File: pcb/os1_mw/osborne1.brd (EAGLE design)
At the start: 147 x 100 mm, 19 parts

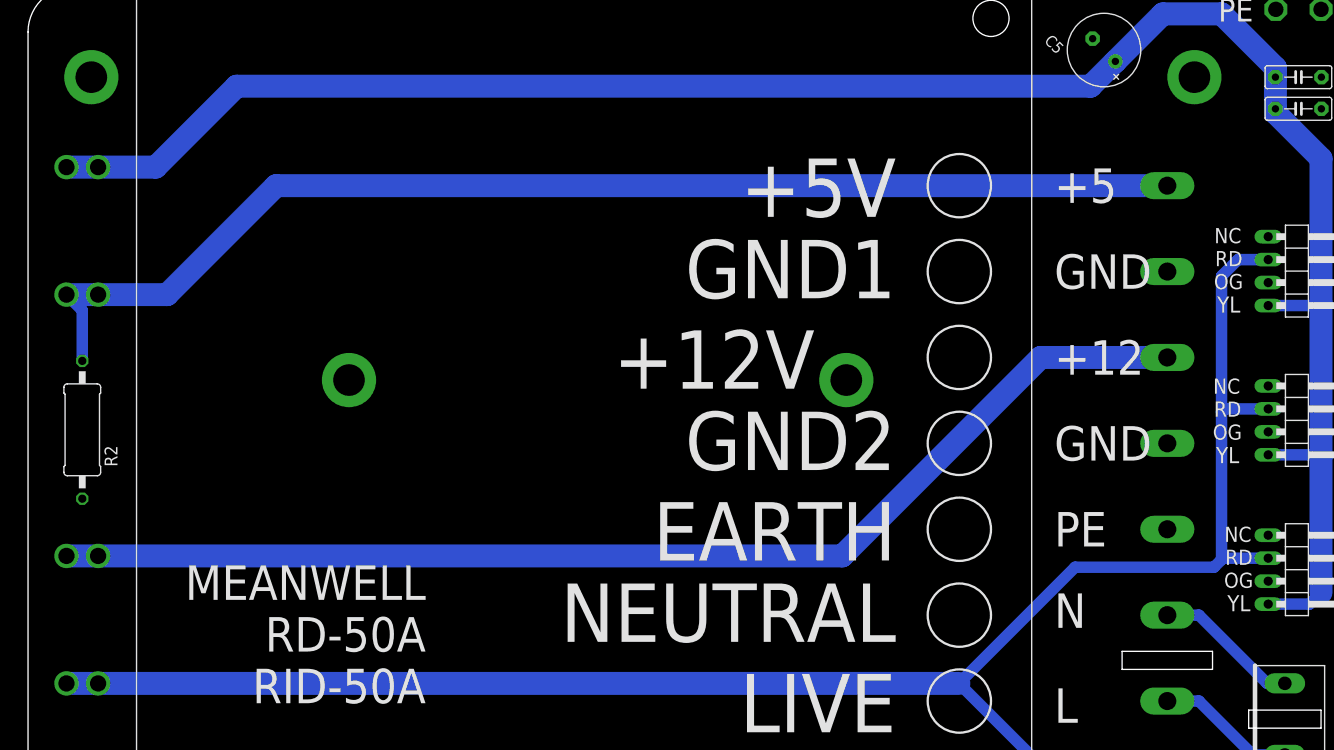
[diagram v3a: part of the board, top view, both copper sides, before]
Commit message: update os1 pcb
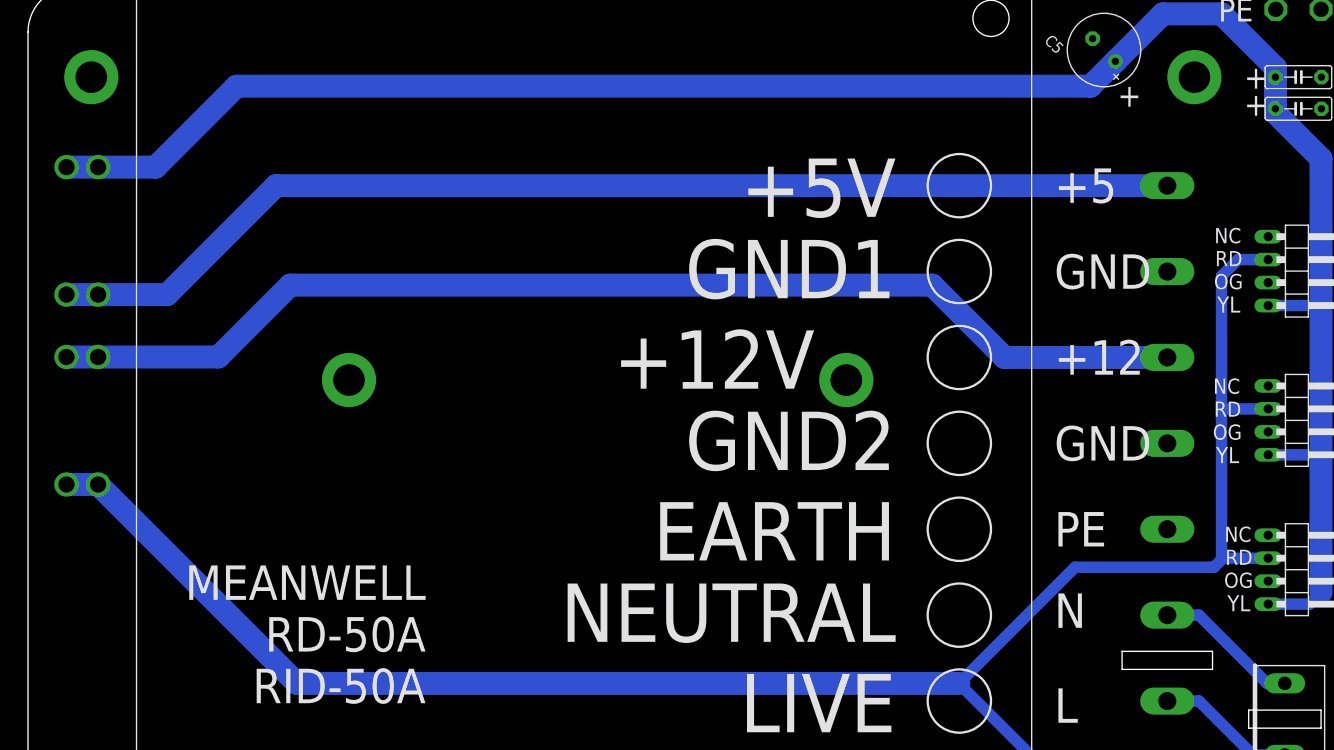
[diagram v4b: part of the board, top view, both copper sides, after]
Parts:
- removed R2: (no value), adafruit_changed:0411/15
- moved U$7 22.0 mm to (6.00, 52.0)
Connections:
- net GND: no longer R2.2
- net N$2: no longer R2.1
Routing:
- net +12V: track 207.7 -> 216.8 mm
- net N$2: track 134.8 -> 126.7 mm
- net N$1: track 130.8 -> 128.4 mm
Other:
- board text added: "+"
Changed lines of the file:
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@@
 <grid distance="1" unitdist="mm" unit="mm" style="lines" multiple="1" display="no" altdistance="1" altunitdist="mil" altunit="mil"/>
 <layers>
-<layer number="1" name="Top" color="4" fill="1" visible="no" active="yes"/>
+<layer number="1" name="Top" color="4" fill="1" visible="yes" active="yes"/>
 <layer number="2" name="Route2" color="16" fill="1" visible="no" active="no"/>
 <layer number="3" name="Route3" color="17" fill="1" visible="no" active="no"/>
@@
 <layer number="19" name="Unrouted" color="6" fill="1" visible="yes" active="yes"/>
 <layer number="20" name="Dimension" color="24" fill="1" visible="yes" active="yes"/>
-<layer number="21" name="tPlace" color="7" fill="1" visible="no" active="yes"/>
+<layer number="21" name="tPlace" color="7" fill="1" visible="yes" active="yes"/>
 <layer number="22" name="bPlace" color="7" fill="1" visible="yes" active="yes"/>
-<layer number="23" name="tOrigins" color="15" fill="1" visible="no" active="yes"/>
+<layer number="23" name="tOrigins" color="15" fill="1" visible="yes" active="yes"/>
 <layer number="24" name="bOrigins" color="15" fill="1" visible="yes" active="yes"/>
-<layer number="25" name="tNames" color="7" fill="1" visible="no" active="yes"/>
+<layer number="25" name="tNames" color="7" fill="1" visible="yes" active="yes"/>
 <layer number="26" name="bNames" color="7" fill="1" visible="yes" active="yes"/>
-<layer number="27" name="tValues" color="7" fill="1" visible="no" active="yes"/>
-<layer number="28" name="bValues" color="7" fill="1" visible="no" active="yes"/>
+<layer number="27" name="tValues" color="7" fill="1" visible="yes" active="yes"/>
+<layer number="28" name="bValues" color="7" fill="1" visible="yes" active="yes"/>
 <layer number="29" name="tStop" color="7" fill="3" visible="no" active="yes"/>
 <layer number="30" name="bStop" color="7" fill="6" visible="no" active="yes"/>
@@
 <layer number="37" name="tTest" color="7" fill="1" visible="no" active="yes"/>
 <layer number="38" name="bTest" color="7" fill="1" visible="no" active="yes"/>
-<layer number="39" name="tKeepout" color="4" fill="11" visible="no" active="yes"/>
+<layer number="39" name="tKeepout" color="4" fill="11" visible="yes" active="yes"/>
 <layer number="40" name="bKeepout" color="1" fill="11" visible="yes" active="yes"/>
-<layer number="41" name="tRestrict" color="4" fill="10" visible="no" active="yes"/>
+<layer number="41" name="tRestrict" color="4" fill="10" visible="yes" active="yes"/>
 <layer number="42" name="bRestrict" color="1" fill="10" visible="yes" active="yes"/>
 <layer number="43" name="vRestrict" color="2" fill="10" visible="no" active="yes"/>
@@
 <layer number="49" name="Reference" color="7" fill="1" visible="no" active="yes"/>
 <layer number="50" name="dxf" color="7" fill="1" visible="no" active="no"/>
-<layer number="51" name="tDocu" color="7" fill="1" visible="no" active="yes"/>
+<layer number="51" name="tDocu" color="7" fill="1" visible="yes" active="yes"/>
 <layer number="52" name="bDocu" color="7" fill="1" visible="yes" active="yes"/>
 <layer number="53" name="tGND_GNDA" color="7" fill="1" visible="no" active="no"/>
@@
 <text x="113.5" y="78" size="3.81" layer="25" align="center-left">+5</text>
 <polygon width="1.27" layer="41">
+<vertex x="1.75" y="61.5"/>
+<vertex x="10.25" y="61.5"/>
+<vertex x="10.25" y="40.5"/>
 <vertex x="1.75" y="40.5"/>
-<vertex x="10.25" y="40.5"/>
-<vertex x="10.25" y="19.5"/>
-<vertex x="1.75" y="19.5"/>
 </polygon>
 <polygon width="1.27" layer="41">
@@
 <rectangle x1="135" y1="18" x2="143" y2="20" layer="46"/>
 <rectangle x1="121" y1="24.5" x2="131" y2="26.5" layer="46"/>
-<text x="12.096" y="30.002" size="3.81" layer="26" rot="MR90" align="center">12V 3A</text>
+<text x="13.096" y="52.002" size="3.81" layer="26" rot="MR90" align="center">12V 3A</text>
 <text x="144.5" y="24" size="3.81" layer="25" align="center-left">N</text>
 <text x="144.5" y="14.5" size="3.81" layer="25" align="center-left">L</text>
@@
 <wire x1="141" y1="26" x2="139" y2="26" width="0.508" layer="22"/>
 <wire x1="139" y1="26" x2="132" y2="33" width="0.508" layer="22"/>
+<text x="120.5" y="88" size="2.54" layer="25" align="center-left">+</text>
+<text x="134.5" y="90" size="2.54" layer="25" align="center-left">+</text>
+<text x="134.5" y="87" size="2.54" layer="25" align="center-left">+</text>
 </plain>
 <attributes>
@@
 </element>
 <element name="JP4" library="appleii" package="1X04" value="" x="119.25" y="3.75" smashed="yes" rot="R180"/>
-<element name="R2" library="adafruit_changed" package="0411/15" value="" x="6" y="51" smashed="yes" rot="R270">
-<attribute name="NAME" x="9.889" y="46.92" size="1.4224" layer="25" ratio="10" rot="R90"/>
-<attribute name="VALUE" x="5.365" y="54.5814" size="1.27" layer="27" ratio="10" rot="R270"/>
-</element>
 <element name="U$3" library="os1" package="TERMINAL9500_MAINS" value="TERM_RD50_MAINS" x="126" y="78" smashed="yes" rot="R270"/>
 <element name="U$2" library="396_conn" package="396_2P_LIVE" value="396_2P_LIVE" x="139" y="19" smashed="yes" rot="R90"/>
-<element name="U$7" library="atx_power_control" package="FUSE_HOLDER_3IN1" value="CAR_FUSE_HOLDER3IN1" x="6" y="30" smashed="yes" rot="MR90"/>
+<element name="U$7" library="atx_power_control" package="FUSE_HOLDER_3IN1" value="CAR_FUSE_HOLDER3IN1" x="6" y="52" smashed="yes" rot="MR90"/>
 </elements>
 <signals>
@@
 <contactref element="U$4" pad="P$1"/>
 <contactref element="U$5" pad="P$1"/>
-<contactref element="R2" pad="2"/>
 <contactref element="U$1" pad="P$2"/>
 <contactref element="U$1" pad="P$1"/>
@@
 <contactref element="U$7" pad="A1"/>
 <contactref element="U$7" pad="A0"/>
-<wire x1="4.25" y1="22.95" x2="7.75" y2="22.95" width="2.54" layer="16"/>
-<wire x1="7.75" y1="22.95" x2="102.95" y2="22.95" width="2.54" layer="16"/>
+<wire x1="4.25" y1="44.95" x2="7.75" y2="44.95" width="2.54" layer="16"/>
 <wire x1="102.95" y1="22.95" x2="120.52" y2="5.38" width="1.27" layer="16"/>
 <wire x1="120.52" y1="5.38" x2="120.52" y2="3.75" width="1.27" layer="16"/>
 <wire x1="131.16" y1="35.8" x2="115.8" y2="35.8" width="1.27" layer="16"/>
 <wire x1="115.8" y1="35.8" x2="102.95" y2="22.95" width="1.27" layer="16"/>
+<wire x1="7.75" y1="44.95" x2="29.75" y2="22.95" width="2.54" layer="16"/>
+<wire x1="29.75" y1="22.95" x2="102.95" y2="22.95" width="2.54" layer="16"/>
 </signal>
 <signal name="N$2">
@@
 <contactref element="U$9" pad="B0"/>
 <wire x1="15.386" y1="65.95" x2="27.436" y2="78" width="2.54" layer="16"/>
-<contactref element="R2" pad="1"/>
 <wire x1="15.386" y1="65.95" x2="7.75" y2="65.95" width="2.54" layer="16"/>
 <wire x1="7.75" y1="65.95" x2="4.25" y2="65.95" width="2.54" layer="16"/>
 <contactref element="U$3" pad="P$1"/>
 <wire x1="27.436" y1="78" x2="126" y2="78" width="2.54" layer="16"/>
-<wire x1="6" y1="58.62" x2="6" y2="64.2" width="1.27" layer="16"/>
-<wire x1="6" y1="64.2" x2="4.25" y2="65.95" width="1.27" layer="16"/>
 </signal>
 <signal name="+5V">
@@
 <contactref element="U$7" pad="B0"/>
 <contactref element="U$7" pad="B1"/>
-<wire x1="126" y1="59" x2="112" y2="59" width="2.54" layer="16"/>
-<wire x1="90.05" y1="37.05" x2="7.75" y2="37.05" width="2.54" layer="16"/>
-<wire x1="112" y1="59" x2="90.05" y2="37.05" width="2.54" layer="16"/>
-<wire x1="7.75" y1="37.05" x2="4.25" y2="37.05" width="2.54" layer="16"/>
+<wire x1="7.75" y1="59.05" x2="4.25" y2="59.05" width="2.54" layer="16"/>
+<wire x1="108" y1="59" x2="100" y2="67" width="2.54" layer="16"/>
+<wire x1="100" y1="67" x2="29" y2="67" width="2.54" layer="16"/>
+<wire x1="21.05" y1="59.05" x2="7.75" y2="59.05" width="2.54" layer="16"/>
+<wire x1="126" y1="59" x2="108" y2="59" width="2.54" layer="16"/>
+<wire x1="29" y1="67" x2="21.05" y2="59.05" width="2.54" layer="16"/>
 </signal>
 <signal name="N$3">

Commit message: adjust PCB
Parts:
- moved C4 7.00 mm to (140.5, 83.0)
- moved C6 7.00 mm to (140.5, 79.5)
- moved TP1 3.16 mm to (139.0, 94.5)
- moved TP2 3.16 mm to (144.0, 94.5)
- moved JP2 2.24 mm to (140.0, 37.5)
- moved JP3 1.41 mm to (140.0, 53.0)
- moved JP1 1.00 mm to (140.0, 68.5)
- turned C5 to 90 degrees
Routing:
- net +5V: track 221.6 -> 217.2 mm
- net +12V: track 216.8 -> 213.8 mm
